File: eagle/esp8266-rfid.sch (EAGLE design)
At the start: 18 parts, among them J1 USB-MICROB", U1 esp-12

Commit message: EAGLE + http push
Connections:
- removed net +5V: U$1.5V, U$1.RES
- removed net N$3: J1.VBUS, T1.VIN
- new net VBUS: J1.VBUS, T1.VIN, U$1.5V, U$1.RES
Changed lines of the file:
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@@
 <part name="R2" library="rcl" deviceset="R-EU_" device="R0603" value="100"/>
 <part name="GND3" library="supply1" deviceset="GND" device=""/>
-<part name="SUPPLY2" library="supply2" deviceset="+5V" device=""/>
 <part name="GND4" library="supply1" deviceset="GND" device=""/>
 <part name="RED_LED" library="wirepad" deviceset="WIREPAD" device="SMD1,27-254" value="WIREPADSMD1,27-254"/>
@@
 <part name="PAUSE_BUTTON" library="wirepad" deviceset="WIREPAD" device="SMD1,27-254" value="WIREPADSMD1,27-254"/>
 <part name="3.3V" library="wirepad" deviceset="WIREPAD" device="SMD1,27-254" value="WIREPADSMD1,27-254"/>
-<part name="SUPPLY3" library="supply2" deviceset="+5V" device=""/>
 <part name="GND5" library="supply1" deviceset="GND" device=""/>
 <part name="GND" library="wirepad" deviceset="WIREPAD" device="SMD1,27-254" value="WIREPADSMD1,27-254"/>
@@
 <instance part="R2" gate="G$1" x="35.56" y="68.58" rot="R90"/>
 <instance part="GND3" gate="1" x="-149.86" y="50.8" rot="R180"/>
-<instance part="SUPPLY2" gate="+5V" x="-109.22" y="53.34" rot="R270"/>
 <instance part="GND4" gate="1" x="60.96" y="58.42" rot="R90"/>
 <instance part="RED_LED" gate="G$1" x="27.94" y="91.44" rot="R270"/>
@@
 <instance part="PAUSE_BUTTON" gate="G$1" x="35.56" y="30.48" rot="R90"/>
 <instance part="3.3V" gate="G$1" x="-15.24" y="27.94" rot="R90"/>
-<instance part="SUPPLY3" gate="+5V" x="-154.94" y="45.72" rot="R90"/>
 <instance part="GND5" gate="1" x="-109.22" y="40.64" rot="R90"/>
 <instance part="GND" gate="G$1" x="15.24" y="30.48" rot="R90"/>
@@
 </segment>
 </net>
-<net name="+5V" class="0">
-<segment>
-<pinref part="U$1" gate="G$1" pin="5V"/>
-<pinref part="SUPPLY2" gate="+5V" pin="+5V"/>
-<wire x1="-116.84" y1="53.34" x2="-111.76" y2="53.34" width="0.1524" layer="91"/>
-</segment>
-<segment>
-<pinref part="U$1" gate="G$1" pin="RES"/>
-<pinref part="SUPPLY3" gate="+5V" pin="+5V"/>
-<wire x1="-147.32" y1="45.72" x2="-152.4" y2="45.72" width="0.1524" layer="91"/>
-</segment>
-</net>
 <net name="N$7" class="0">
 <segment>
@@
 </segment>
 </net>
-<net name="N$3" class="0">
-<segment>
-<pinref part="J1" gate="G$1" pin="VBUS"/>
-<pinref part="T1" gate="A" pin="VIN"/>
-<wire x1="-154.94" y1="83.82" x2="-121.92" y2="83.82" width="0.1524" layer="91"/>
-</segment>
-</net>
 <net name="N$8" class="0">
 <segment>
@@
 </segment>
 </net>
+<net name="VBUS" class="0">
+<segment>
+<pinref part="U$1" gate="G$1" pin="RES"/>
+<wire x1="-147.32" y1="45.72" x2="-152.4" y2="45.72" width="0.1524" layer="91"/>
+</segment>
+<segment>
+<pinref part="J1" gate="G$1" pin="VBUS"/>
+<pinref part="T1" gate="A" pin="VIN"/>
+<wire x1="-154.94" y1="83.82" x2="-121.92" y2="83.82" width="0.1524" layer="91"/>
+</segment>
+<segment>
+<pinref part="U$1" gate="G$1" pin="5V"/>
+<wire x1="-116.84" y1="53.34" x2="-111.76" y2="53.34" width="0.1524" layer="91"/>
+</segment>
+</net>

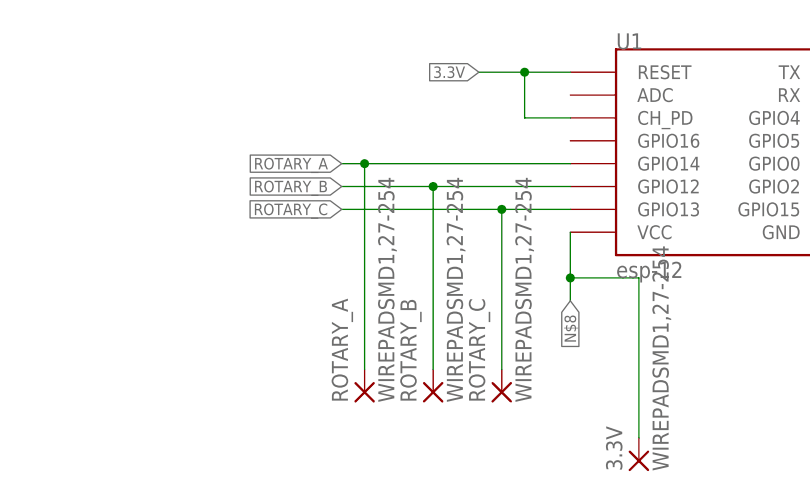
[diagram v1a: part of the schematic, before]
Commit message: EAGLE: rotary fix
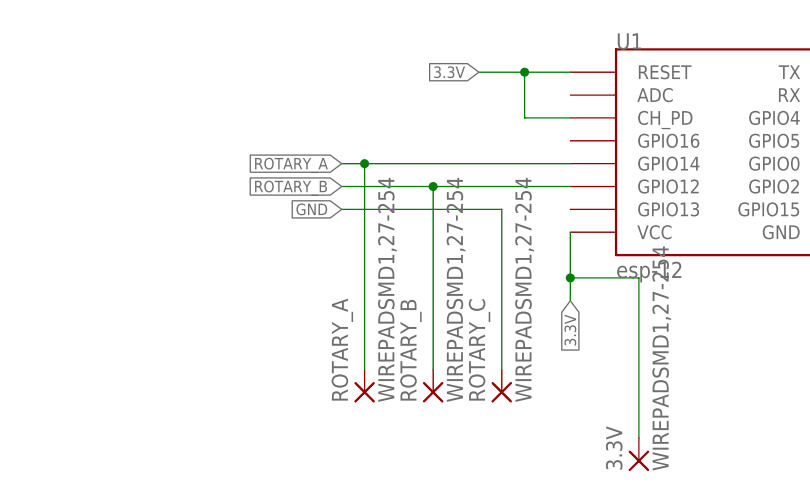
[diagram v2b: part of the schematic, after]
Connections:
- removed net N$8: 3.3V.P, U1.VCC
- removed net ROTARY_C: ROTARY_C.P, U1.GPIO13
- net 3.3V: now also 3.3V.P, U1.VCC
- net GND: now also ROTARY_C.P
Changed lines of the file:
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@@
 <wire x1="55.88" y1="58.42" x2="58.42" y2="58.42" width="0.1524" layer="91"/>
+</segment>
+<segment>
+<label x="-48.26" y="55.88" size="1.27" layer="95" rot="R180" xref="yes"/>
+<pinref part="ROTARY_C" gate="G$1" pin="P"/>
+<wire x1="-30.48" y1="55.88" x2="-48.26" y2="55.88" width="0.1524" layer="91"/>
+<wire x1="-30.48" y1="38.1" x2="-30.48" y2="55.88" width="0.1524" layer="91"/>
 </segment>
 </net>
@@
 </segment>
 </net>
-<net name="ROTARY_C" class="0">
-<segment>
-<pinref part="U1" gate="G$1" pin="GPIO13"/>
-<wire x1="-22.86" y1="55.88" x2="-30.48" y2="55.88" width="0.1524" layer="91"/>
-<label x="-48.26" y="55.88" size="1.27" layer="95" rot="R180" xref="yes"/>
-<pinref part="ROTARY_C" gate="G$1" pin="P"/>
-<wire x1="-30.48" y1="55.88" x2="-48.26" y2="55.88" width="0.1524" layer="91"/>
-<wire x1="-30.48" y1="38.1" x2="-30.48" y2="55.88" width="0.1524" layer="91"/>
-<junction x="-30.48" y="55.88"/>
-</segment>
-</net>
 <net name="ROTARY_A" class="0">
 <segment>
@@
 <label x="-88.9" y="86.36" size="1.778" layer="95" xref="yes"/>
 </segment>
-</net>
-<net name="N$1" class="0">
-<segment>
-<pinref part="U1" gate="G$1" pin="GPIO0"/>
-<pinref part="U$2" gate="G$1" pin="COM"/>
-<wire x1="10.16" y1="60.96" x2="40.64" y2="60.96" width="0.1524" layer="91"/>
-</segment>
-</net>
-<net name="N$8" class="0">
 <segment>
 <pinref part="U1" gate="G$1" pin="VCC"/>
@@
 </segment>
 </net>
+<net name="N$1" class="0">
+<segment>
+<pinref part="U1" gate="G$1" pin="GPIO0"/>
+<pinref part="U$2" gate="G$1" pin="COM"/>
+<wire x1="10.16" y1="60.96" x2="40.64" y2="60.96" width="0.1524" layer="91"/>
+</segment>
+</net>

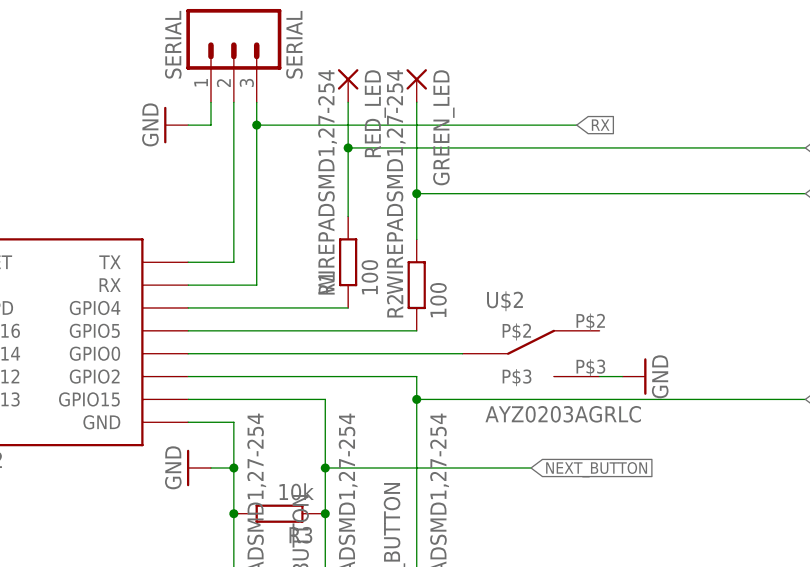
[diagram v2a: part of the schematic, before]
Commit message: EAGLE: resistance value update
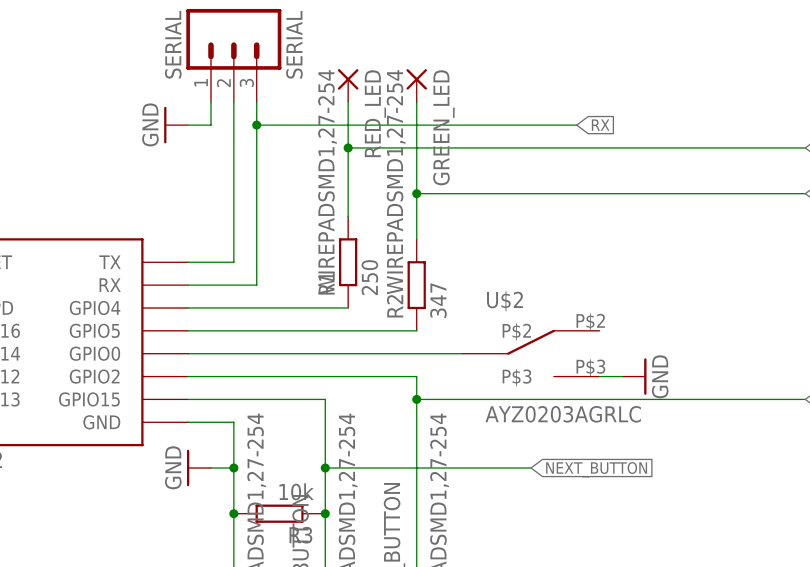
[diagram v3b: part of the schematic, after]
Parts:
- R1: value 100 -> 250
- R2: value 100 -> 347
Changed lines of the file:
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@@
 <part name="J1" library="SparkFun-Connectors" deviceset="USB-MICROB" device="&quot;"/>
 <part name="GND1" library="supply1" deviceset="GND" device=""/>
-<part name="R1" library="rcl" deviceset="R-EU_" device="R0603" value="100"/>
-<part name="R2" library="rcl" deviceset="R-EU_" device="R0603" value="100"/>
+<part name="R1" library="rcl" deviceset="R-EU_" device="R0603" value="250"/>
+<part name="R2" library="rcl" deviceset="R-EU_" device="R0603" value="347"/>
 <part name="GND3" library="supply1" deviceset="GND" device=""/>
 <part name="GND4" library="supply1" deviceset="GND" device=""/>
